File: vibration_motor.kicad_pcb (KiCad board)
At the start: 2 copper layers, 15.2 x 9.3 mm, 5 parts, among them J3 Conn_01x03, U3 ECH8693R-TL-W, U4 C0720B001F

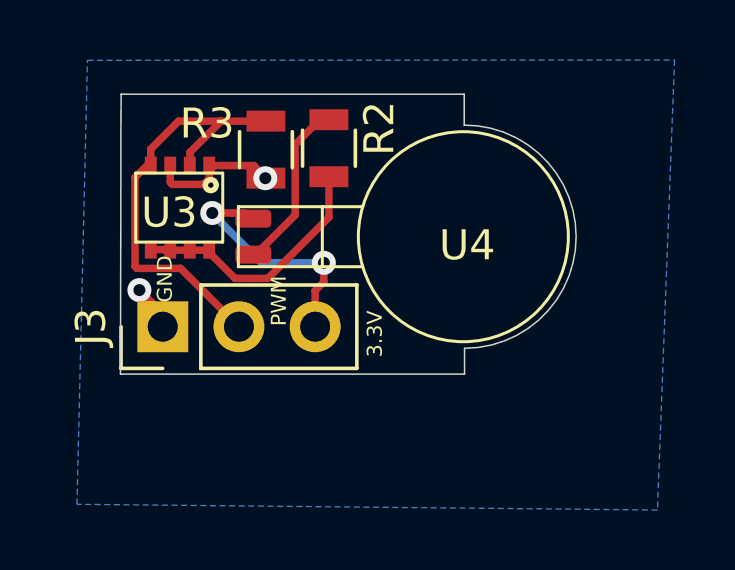
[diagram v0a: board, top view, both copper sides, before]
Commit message: Rework and rename parts
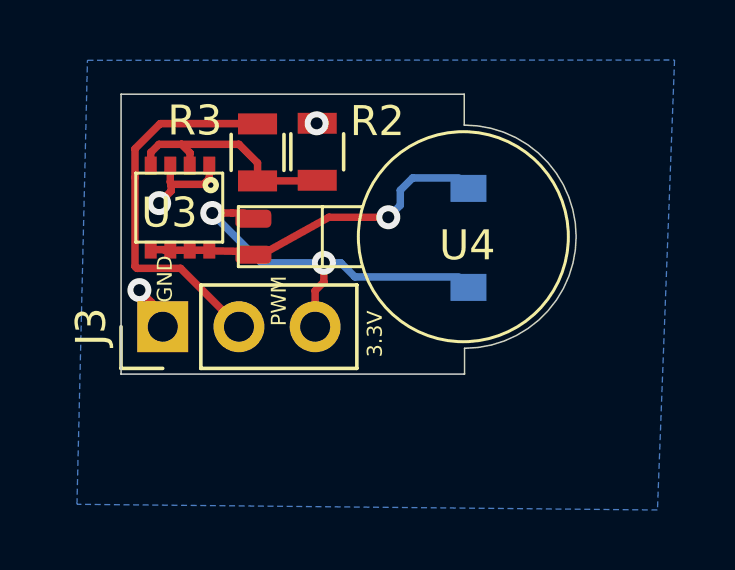
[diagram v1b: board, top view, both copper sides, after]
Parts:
- added D3: 1N4148, Diodes_SMD:D_SOD-123, B.Cu at (130.6, 112.7)
- moved R3 2.38 mm to (123.5, 109.9), turned to 270 degrees
- moved R2 1.71 mm to (125.5, 109.8), turned to 270 degrees
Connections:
- R2 pad 2: MOTOR_PWM -> Net-(R2-Pad2)
- R3 pad 1: Net-(R3-Pad1) -> MOTOR_PWM
- R3 pad 2: Net-(R3-Pad2) -> Net-(R2-Pad2)
- U3 pad 2: MOTOR_PWM -> Net-(R2-Pad2)
- U3 pad 4: MOTOR_PWM -> Net-(R2-Pad2)
- U3 pad 5: Net-(R3-Pad1) -> Net-(D3-Pad2)
- U3 pad 6: Net-(R3-Pad1) -> Net-(D3-Pad2)
- U3 pad 7: Net-(R3-Pad1) -> Net-(D3-Pad2)
- U3 pad 8: Net-(R3-Pad1) -> Net-(D3-Pad2)
- U4 pad 2: Net-(R3-Pad2) -> Net-(D3-Pad2)
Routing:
- net Net-(D3-Pad2): track 0.00 -> 10.8 mm, vias 0 -> 1
- net Net-(R3-Pad1): track 8.55 -> 0.00 mm
- net Net-(R2-Pad2): track 0.00 -> 7.74 mm
- net Net-(R3-Pad2): track 5.60 -> 0.00 mm
- net +3.3: track 7.67 -> 12.4 mm
- net MOTOR_PWM: track 14.6 -> 12.6 mm
- net (GND): track 5.87 -> 4.59 mm, vias 2 -> 3
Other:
- outline, holes or cut-outs redrawn
